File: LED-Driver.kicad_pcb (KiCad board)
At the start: 2 copper layers, 0 parts

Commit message: Add an initial PCB and swap out the barrel jack
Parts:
- added J2: Barrel_Jack_Switch, Connector_BarrelJack:BarrelJack_CUI_PJ-102AH_Horizontal, F.Cu at (50.7, 27.0)
- added U1: Pico, RPi_Pico:RPi_Pico_SMD_TH, F.Cu at (26.9, 39.0)
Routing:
- net GND: track 0.00 -> 15.3 mm

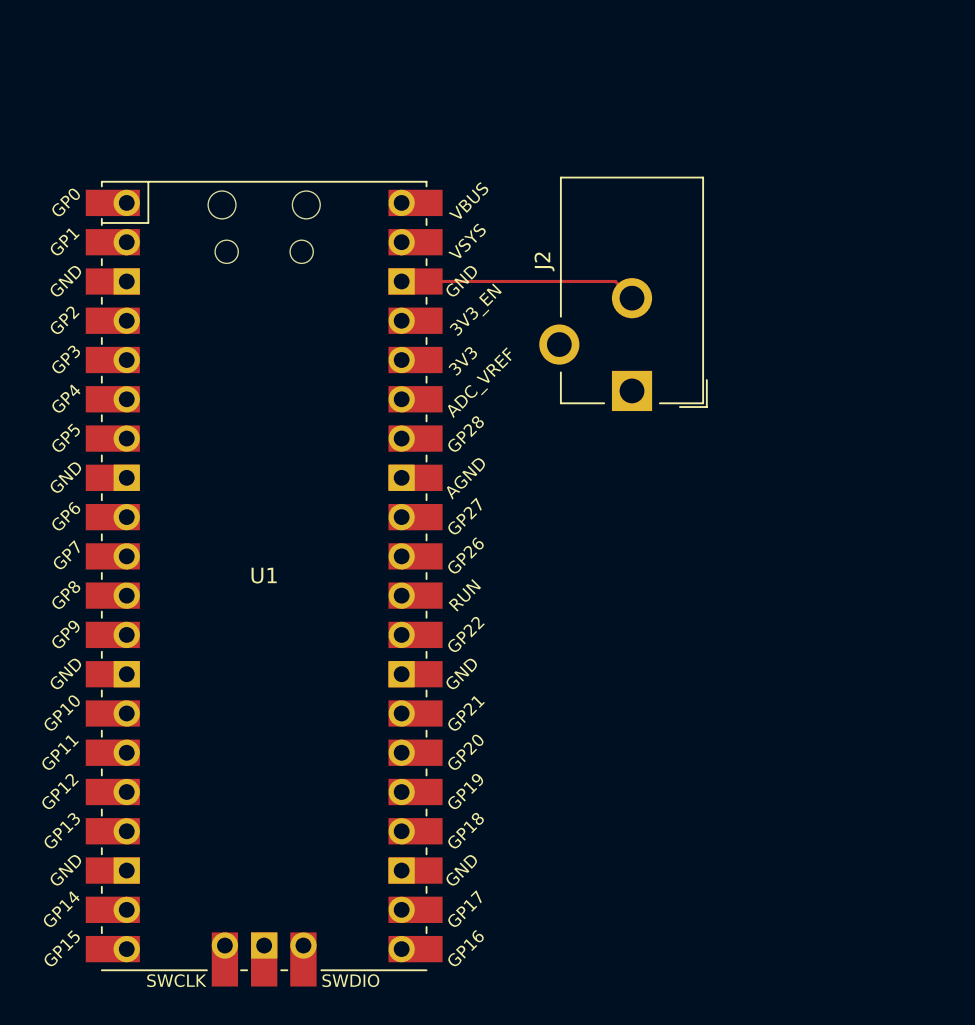
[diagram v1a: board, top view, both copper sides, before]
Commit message: Add borders to the PCB
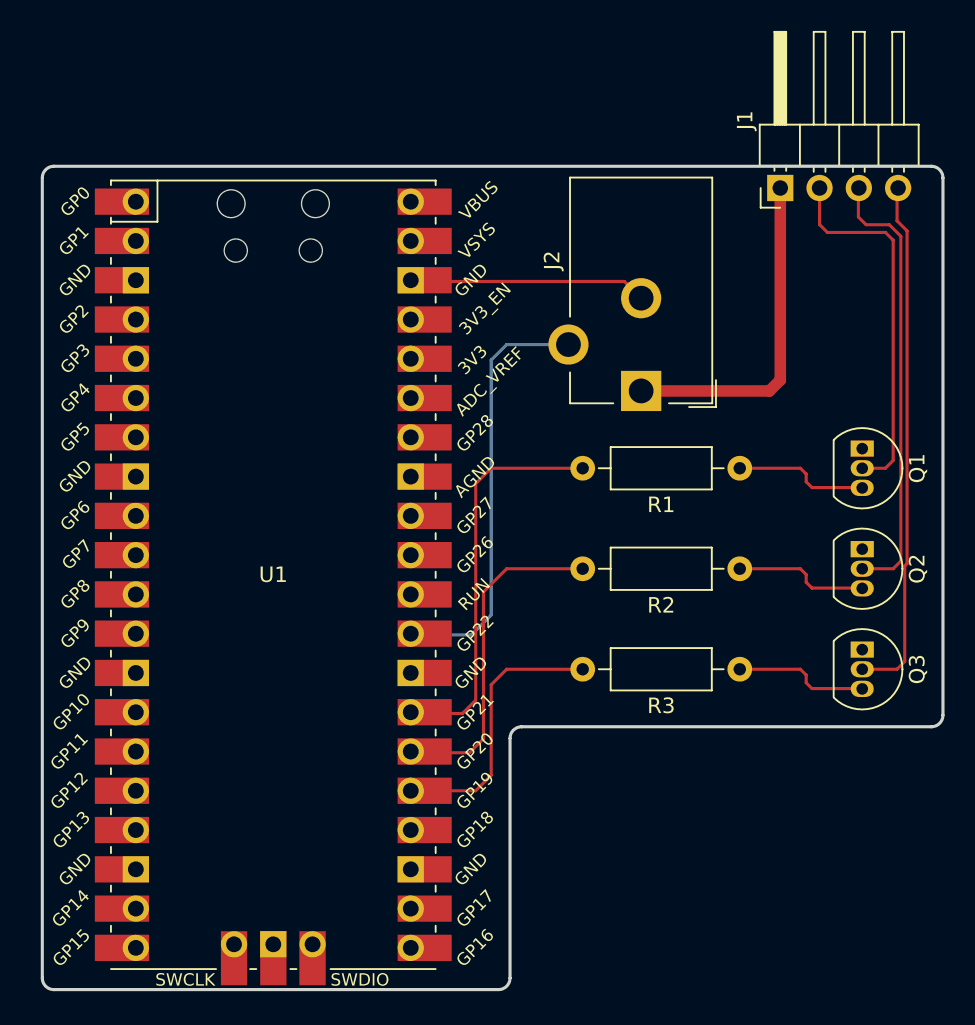
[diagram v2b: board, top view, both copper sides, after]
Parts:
- added J1: Conn_01x04, Connector_PinHeader_2.54mm:PinHeader_1x04_P2.54mm_Horizontal, F.Cu at (60.3, 13.9)
- added Q1: NTE289, Package_TO_SOT_THT:TO-92_Inline, F.Cu at (65.6, 30.7)
- added Q2: NTE289, Package_TO_SOT_THT:TO-92_Inline, F.Cu at (65.6, 37.2)
- added Q3: NTE289, Package_TO_SOT_THT:TO-92_Inline, F.Cu at (65.6, 43.7)
- added R1: R, Resistor_THT:R_Axial_DIN0207_L6.3mm_D2.5mm_P10.16mm_Horizontal, F.Cu at (57.7, 32.0)
- added R2: R, Resistor_THT:R_Axial_DIN0207_L6.3mm_D2.5mm_P10.16mm_Horizontal, F.Cu at (57.7, 38.5)
- added R3: R, Resistor_THT:R_Axial_DIN0207_L6.3mm_D2.5mm_P10.16mm_Horizontal, F.Cu at (57.7, 45.0)
- moved U1 0.60 mm to (27.5, 38.9)
- moved J2 0.59 mm to (51.3, 27.0)
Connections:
- J2 pad 3: unconnected-(J2-Pad3) -> Net-(U1-GPIO22)
- U1 pad 1: Net-(U1-GPIO0) -> unconnected-(U1-GPIO0-Pad1)
- U1 pad 2: Net-(U1-GPIO1) -> unconnected-(U1-GPIO1-Pad2)
- U1 pad 25: unconnected-(U1-GPIO19-Pad25) -> Net-(U1-GPIO19)
- U1 pad 26: unconnected-(U1-GPIO20-Pad26) -> Net-(U1-GPIO20)
- U1 pad 27: unconnected-(U1-GPIO21-Pad27) -> Net-(U1-GPIO21)
- U1 pad 29: unconnected-(U1-GPIO22-Pad29) -> Net-(U1-GPIO22)
- U1 pad 4: Net-(U1-GPIO2) -> unconnected-(U1-GPIO2-Pad4)
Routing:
- net Net-(J1-Pin_4): track 0.00 -> 33.9 mm
- net Net-(J1-Pin_3): track 0.00 -> 28.9 mm
- net Net-(U1-GPIO22): track 0.00 -> 27.6 mm
- net Net-(U1-GPIO21): track 0.00 -> 25.9 mm
- net Net-(J1-Pin_2): track 0.00 -> 21.8 mm
- net +12V: track 0.00 -> 21.7 mm
- net Net-(U1-GPIO20): track 0.00 -> 21.6 mm
- net Net-(U1-GPIO19): track 0.00 -> 17.8 mm
- net Net-(Q1-B): track 0.00 -> 8.74 mm
- net Net-(Q3-B): track 0.00 -> 8.71 mm
- net Net-(Q2-B): track 0.00 -> 8.71 mm
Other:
- board outline added: 58.2 x 53.2 mm
